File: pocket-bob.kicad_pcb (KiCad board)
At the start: 2 copper layers, 104.1 x 58.4 mm, 131 parts, among them J3 Conn_01x18, J4 Conn_01x18, J5 Conn_01x18, J6 Conn_01x18, J7 USB_A, P1 Conn_02x18_Odd_Even, P2 Conn_02x18_Odd_Even, U1 TPD3S014

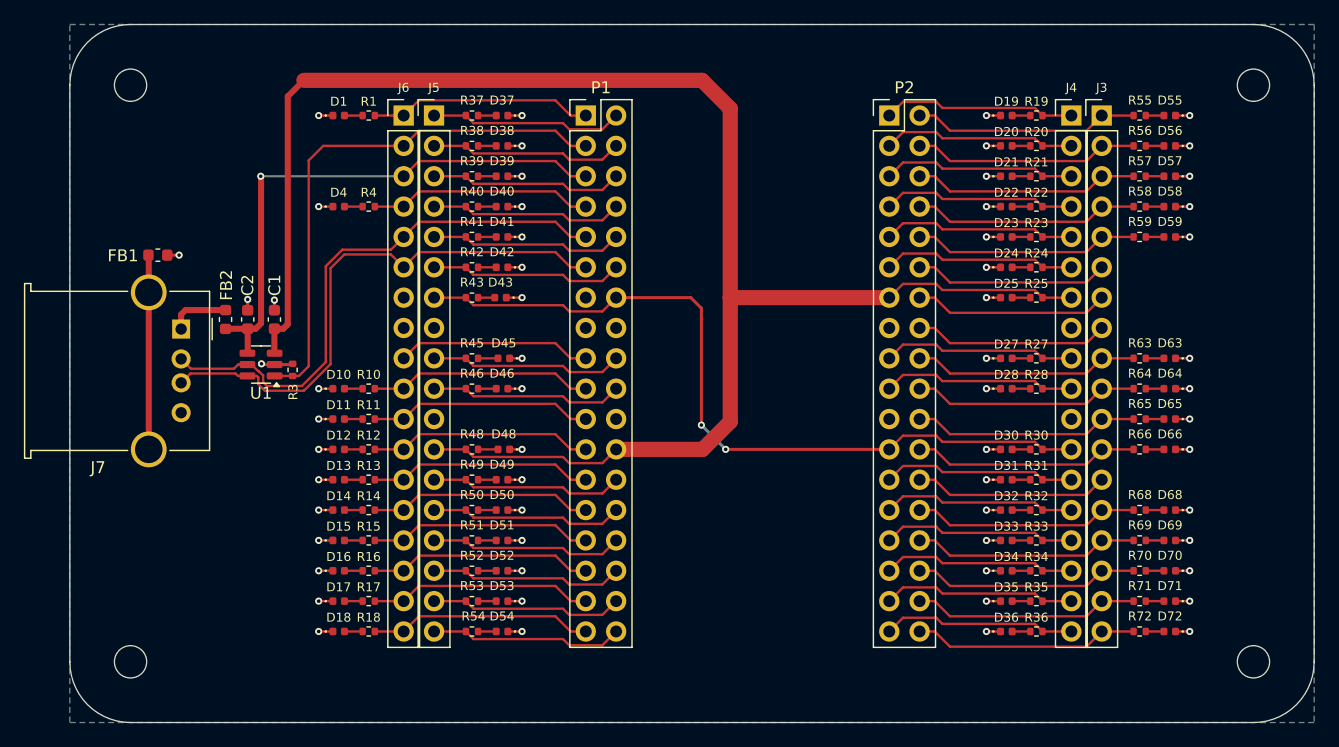
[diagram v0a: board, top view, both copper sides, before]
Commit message: Add pin labels to silkscreen
Signed-off-by: Michael Welling <mwelling79@gmail.com>
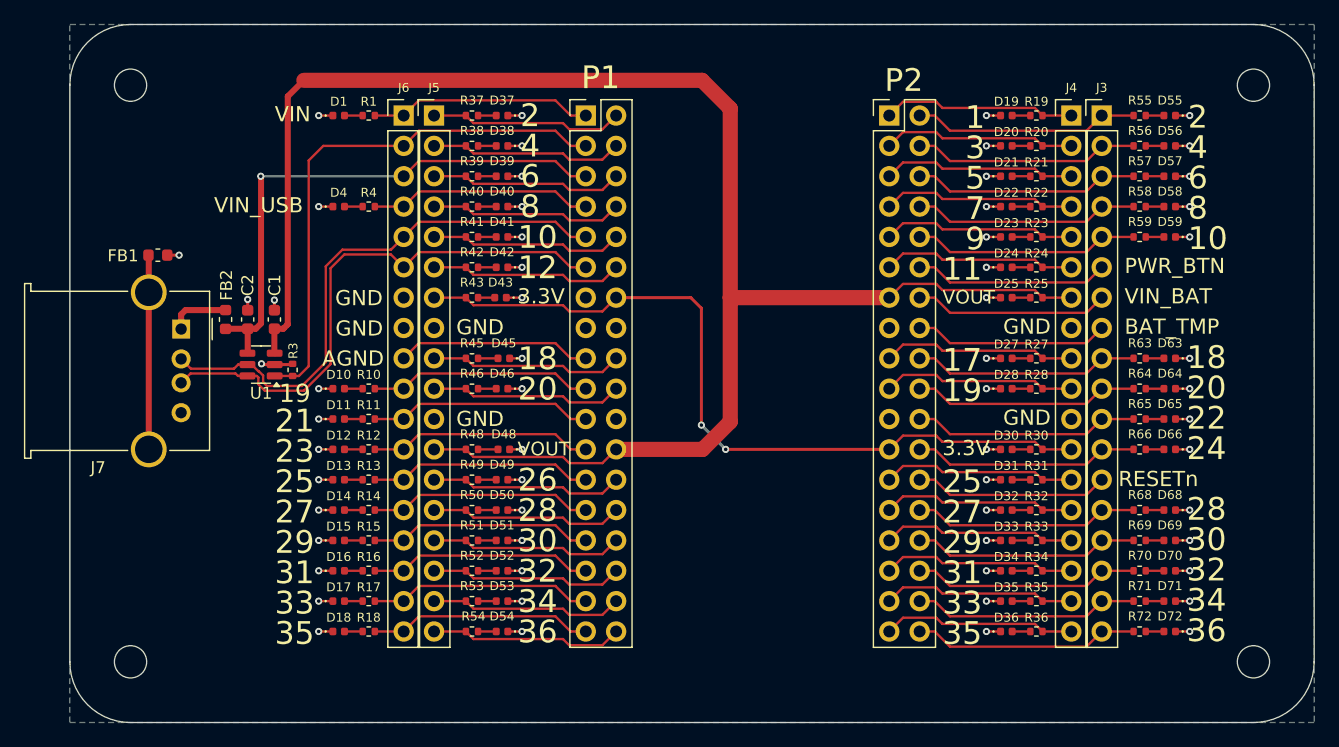
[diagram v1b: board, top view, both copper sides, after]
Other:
- board text added: "1"
- board text added: "10"
- board text added: "11"
- board text added: "12"
- board text added: "17"
- board text added: "18"
- board text added: "19"
- board text added: "2"
- board text added: "20"
- board text added: "21"
- board text added: "22"
- board text added: "23"
- board text added: "24"
- board text added: "25"
- board text added: "26"
- board text added: "27"
- board text added: "28"
- board text added: "29"
- board text added: "3"
- board text added: "3.3V"
- board text added: "30"
- board text added: "31"
- board text added: "32"
- board text added: "33"
- board text added: "34"
- board text added: "35"
- board text added: "36"
- board text added: "4"
- board text added: "5"
- board text added: "6"
- board text added: "7"
- board text added: "8"
- board text added: "9"
- board text added: "AGND"
- board text added: "BAT_TMP"
- board text added: "GND"
- board text added: "PWR_BTN"
- board text added: "RESETn"
- board text added: "VIN"
- board text added: "VIN_BAT"
- board text added: "VIN_USB"
- board text added: "VOUT"

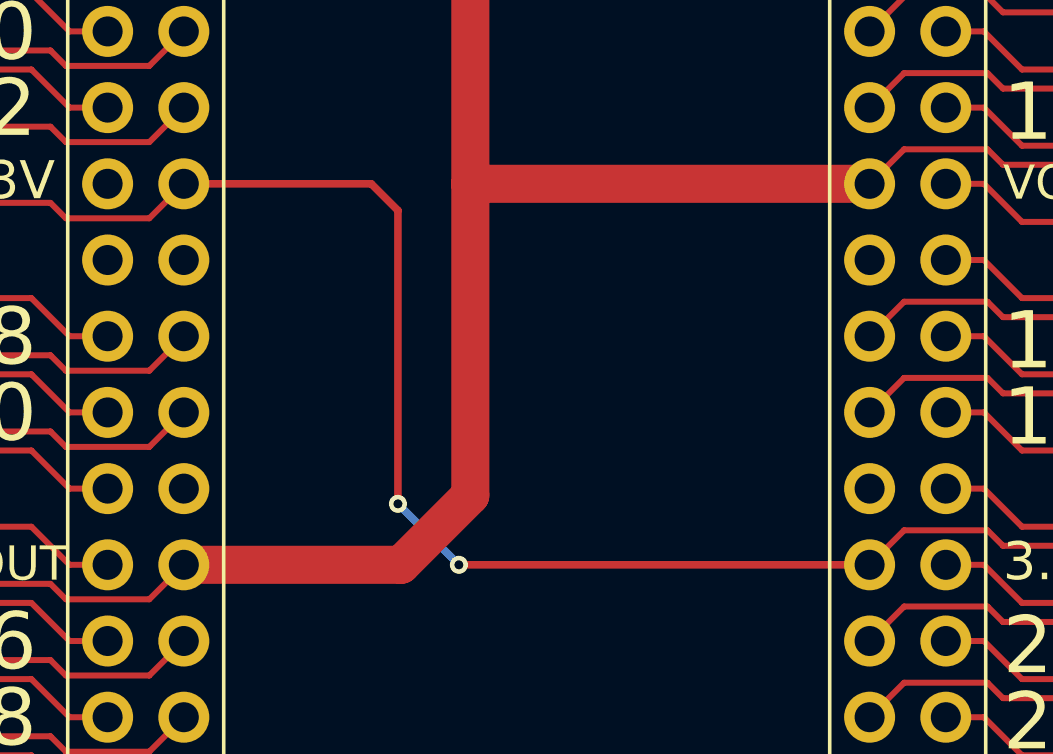
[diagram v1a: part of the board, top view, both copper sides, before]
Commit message: Clean up routing and add mounting holes to sch
Signed-off-by: Michael Welling <mwelling79@gmail.com>
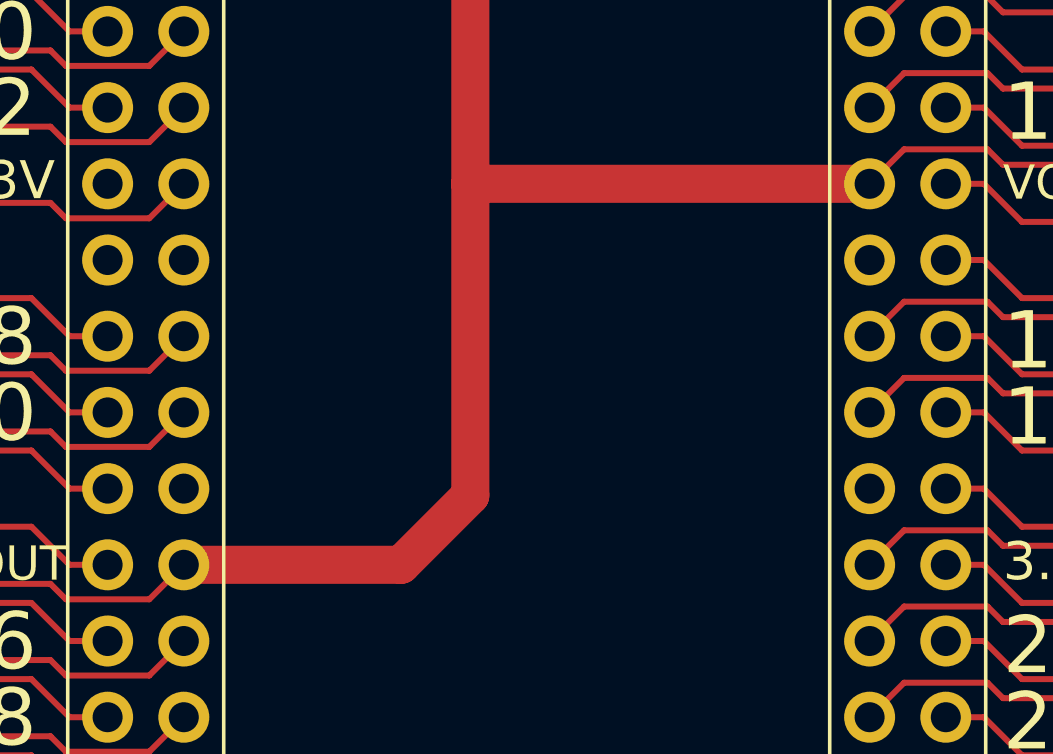
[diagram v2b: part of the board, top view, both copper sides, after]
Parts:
- removed REF** (x4): MountingHole_2.7mm_M2.5, MountingHole:MountingHole_2.7mm_M2.5
- added H1: MountingHole, MountingHole:MountingHole_2.7mm_M2.5, F.Cu at (43.2, 66.0)
- added H2: MountingHole, MountingHole:MountingHole_2.7mm_M2.5, F.Cu at (43.2, 114.3)
- added H3: MountingHole, MountingHole:MountingHole_2.7mm_M2.5, F.Cu at (137.2, 66.0)
- added H4: MountingHole, MountingHole:MountingHole_2.7mm_M2.5, F.Cu at (137.2, 114.3)
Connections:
- J4 pad 12: /3P3V -> /3P3V_1
- P2 pad 23: /3P3V -> /3P3V_1
- R30 pad 2: /3P3V -> /3P3V_1
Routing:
- net /3P3V: track 66.2 -> 16.2 mm, vias 2 -> 0
- net /3P3V_1: track 0.00 -> 16.2 mm
